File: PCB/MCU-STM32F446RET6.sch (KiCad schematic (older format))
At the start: 48 parts, among them J3 20021121-00010C4LF, J4 0475890001-MicroUSBPort, P1 CONN_01X18, P2 CONN_01X18, SW1 B3U-1000P, U3 STM32F446RET6_-_TQFP64, X1 ABM3B8.000MHZB2T, X2 ABS07-32.768KHZ-9-T

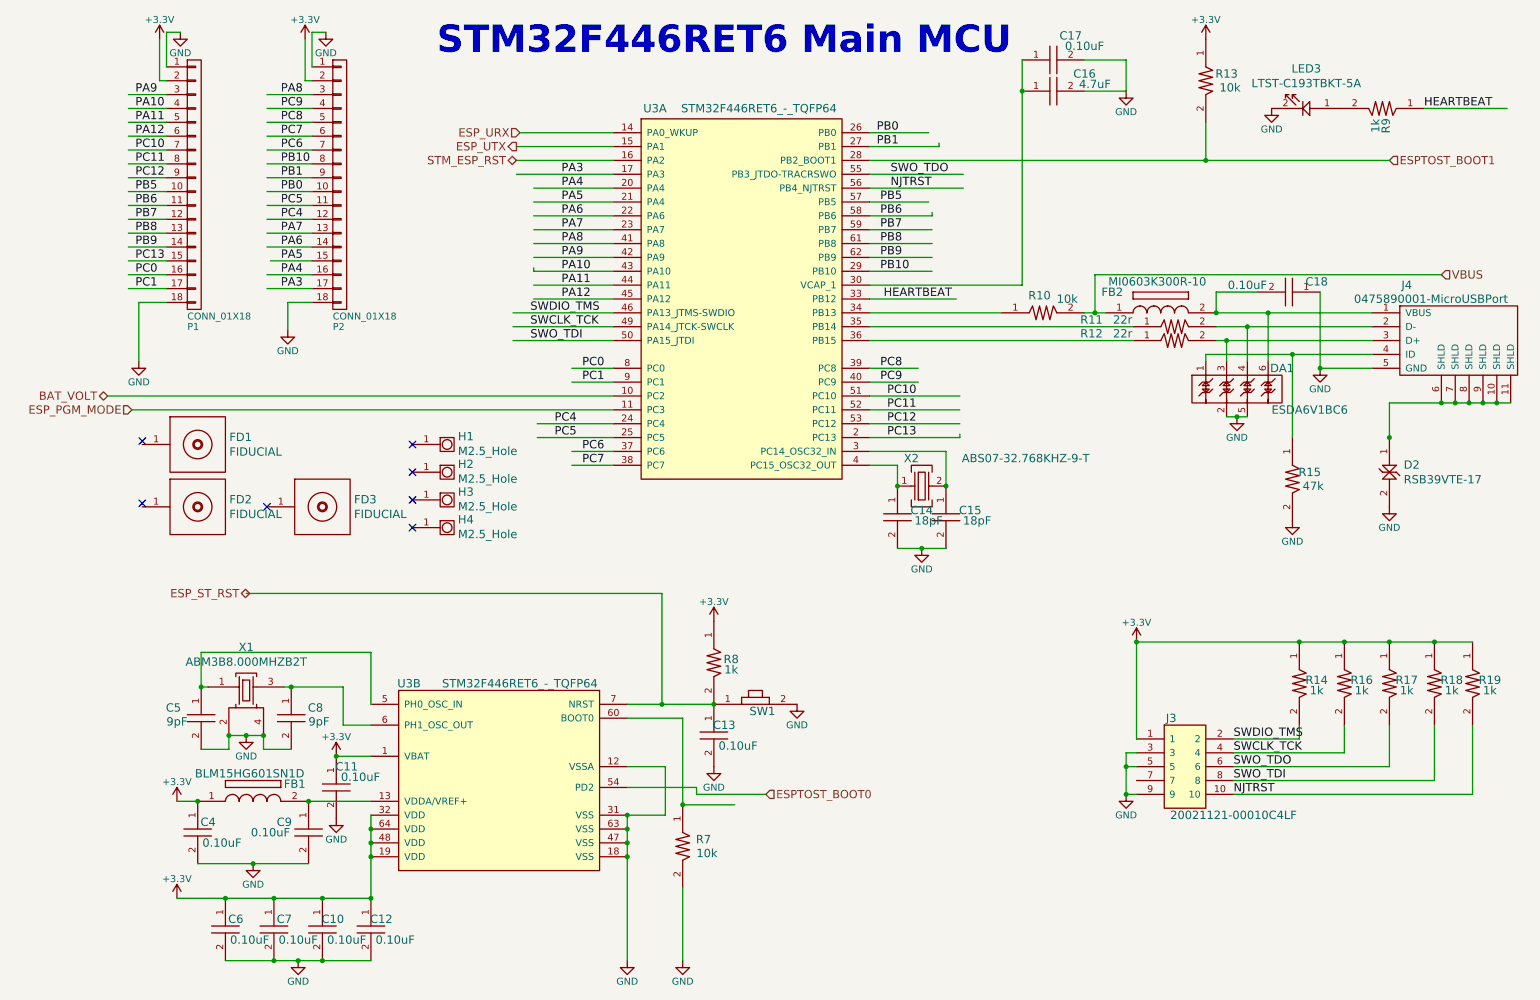
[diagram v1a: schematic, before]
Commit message: Sheets
Hiearchal sheet structure mostly established and linked. Need to
research more on OTA pgoramming with ADF7023 if possible.
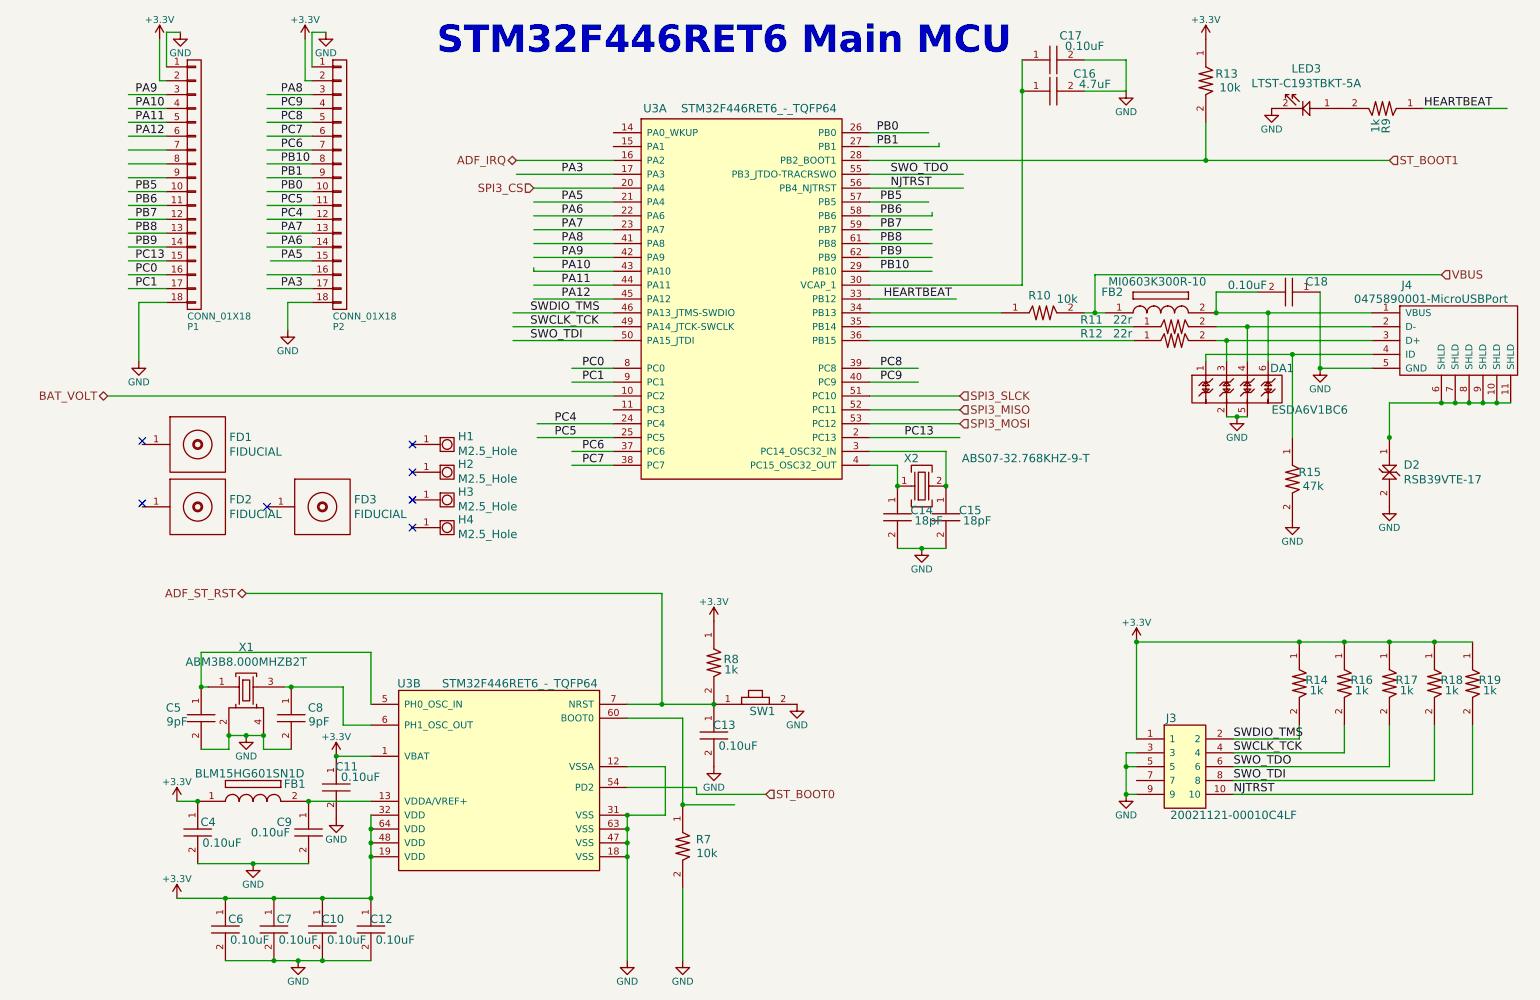
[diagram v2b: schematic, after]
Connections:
- net labels added: ADF_IRQ, ADF_ST_RST, SPI3_CS, SPI3_MISO, SPI3_MOSI, SPI3_SLCK, ST_BOOT0, ST_BOOT1
- net labels removed: ESPTOST_BOOT0, ESPTOST_BOOT1, ESP_PGM_MODE, ESP_ST_RST, ESP_URX, ESP_UTX, PA4, PC10, PC11, PC12, STM_ESP_RST
- wire segments 172 -> 168
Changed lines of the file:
@@
 Comment4 ""
 $EndDescr
-Text HLabel 2000 4775 0    60   BiDi ~ 0
-ESP_ST_RST
+Text HLabel 1975 4775 0    60   BiDi ~ 0
+ADF_ST_RST
 Text HLabel 3925 1650 0    60   BiDi ~ 0
-STM_ESP_RST
-Text HLabel 3925 1550 0    60   Output ~ 0
-ESP_UTX
-Text HLabel 3950 1450 0    60   Input ~ 0
-ESP_URX
-Text HLabel 1150 3450 0    60   Input ~ 0
-ESP_PGM_MODE
+ADF_IRQ
 Text HLabel 10600 2475 2    60   Input ~ 0
 VBUS
@@
 $EndComp
 Text HLabel 5725 6225 2    59   Input ~ 0
-ESPTOST_BOOT0
+ST_BOOT0
 Text HLabel 10225 1650 2    59   Input ~ 0
-ESPTOST_BOOT1
+ST_BOOT1
 Text HLabel 975  3350 0    60   BiDi ~ 0
 BAT_VOLT
@@
 $EndComp
 Wire Wire Line
-	3925 1550 4625 1550
-Wire Wire Line
-	4625 1450 3950 1450
-Wire Wire Line
 	5125 6300 5500 6300
 Wire Wire Line
@@
 Wire Wire Line
 	6475 3550 7125 3550
-Text Label 6600 3350 0    60   ~ 0
-PC10
-Text Label 6600 3550 0    60   ~ 0
-PC12
-Text Label 1175 1575 0    60   ~ 0
-PC10
-Text Label 1175 1775 0    60   ~ 0
-PC12
 $Comp
 L GND #PWR17
@@
 Wire Wire Line
 	4075 3650 4625 3650
-Text Label 4250 1850 0    60   ~ 0
-PA4
 Text Label 4250 1950 0    60   ~ 0
 PA5
@@
 Wire Wire Line
 	4625 3250 4325 3250
-Wire Wire Line
-	1150 3450 4625 3450
-Text Label 1175 1675 0    60   ~ 0
-PC11
 Text Label 4400 3250 0    60   ~ 0
 PC1
@@
 	6475 3650 7125 3650
 Wire Wire Line
-	7125 3650 7125 3625
-Wire Wire Line
 	6475 1550 6975 1550
 Wire Wire Line
@@
 Wire Wire Line
 	6475 1450 6900 1450
-Text Label 6600 3650 0    60   ~ 0
+Text Label 6725 3650 0    60   ~ 0
 PC13
 Text Label 1175 2375 0    60   ~ 0
@@
 	1    0    0    -1
 $EndComp
-Text Label 6600 3450 0    60   ~ 0
-PC11
 Wire Wire Line
 	6475 3450 7125 3450
 Text Label 4250 1750 0    60   ~ 0
 PA3
-Text Label 2225 2475 0    60   ~ 0
-PA4
 Text Label 2225 2575 0    60   ~ 0
 PA3
@@
 Wire Wire Line
 	1125 1175 1400 1175
+Text HLabel 7125 3350 2    60   Input ~ 0
+SPI3_SLCK
+Text HLabel 7125 3450 2    60   Input ~ 0
+SPI3_MISO
+Text HLabel 7125 3550 2    60   Input ~ 0
+SPI3_MOSI
+Text HLabel 4050 1850 0    60   Input ~ 0
+SPI3_CS
 $EndSCHEMATC
